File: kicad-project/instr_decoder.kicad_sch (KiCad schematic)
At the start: 0 parts

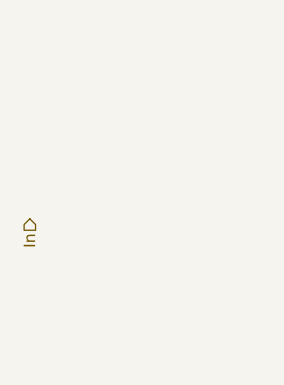
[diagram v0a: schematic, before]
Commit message: update schematic
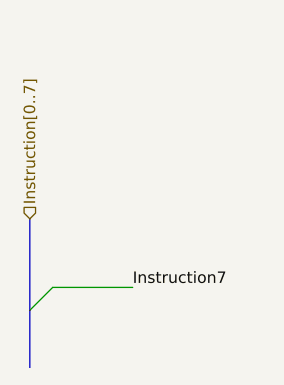
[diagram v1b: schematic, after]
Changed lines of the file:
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@@
 (kicad_sch (version 20211123) (generator eeschema)
   (paper "A4")
-  (hierarchical_label "In" (shape input) (at 152.4 50.8 270)
-    (effects (font (size 1.27 1.27)) (justify right))
+  (bus_entry (at 152.4 60.96) (size 2.54 -2.54)
+    (stroke (width 0) (type default) (color 0 0 0 0))
+  )
+  (bus (pts (xy 152.4 50.8) (xy 152.4 60.96))
+    (stroke (width 0) (type default) (color 0 0 0 0))
+  )
+  (bus (pts (xy 152.4 60.96) (xy 152.4 67.31))
+    (stroke (width 0) (type default) (color 0 0 0 0))
+  )
+  (wire (pts (xy 154.94 58.42) (xy 163.83 58.42))
+    (stroke (width 0) (type default) (color 0 0 0 0))
+  )
+  (label "Instruction7" (at 163.83 58.42 0)
+    (effects (font (size 1.27 1.27)) (justify left bottom))
+  )
+  (hierarchical_label "Instruction[0..7]" (shape input) (at 152.4 50.8 90)
+    (effects (font (size 1.27 1.27)) (justify left))
   )
 )
